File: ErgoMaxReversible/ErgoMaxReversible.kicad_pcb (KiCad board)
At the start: 2 copper layers, 182.8 x 169.2 mm, 106 parts, among them J1 PJ-320A, K1 KEYSW, K10 KEYSW, K11 KEYSW, K12 KEYSW, K13 KEYSW, K14 KEYSW, K15 KEYSW, K16 KEYSW, K17 KEYSW, K18 KEYSW, K19 KEYSW, K2 KEYSW, K20 KEYSW, K21 KEYSW, K22 KEYSW, K23 KEYSW, K24 KEYSW, K25 KEYSW, K26 KEYSW, K27 KEYSW, K28 KEYSW, K29 KEYSW, K3 KEYSW, K30 KEYSW, K31 KEYSW, K32 KEYSW, K33 KEYSW, K34 KEYSW, K35 KEYSW, K36 KEYSW, K37 KEYSW, K38 KEYSW, K39 KEYSW, K4 KEYSW, K40 KEYSW, K41 KEYSW, K42 KEYSW, K43 KEYSW, K44 KEYSW, K5 KEYSW, K6 KEYSW, K7 KEYSW, K8 KEYSW, K9 KEYSW, U1 ProMicro

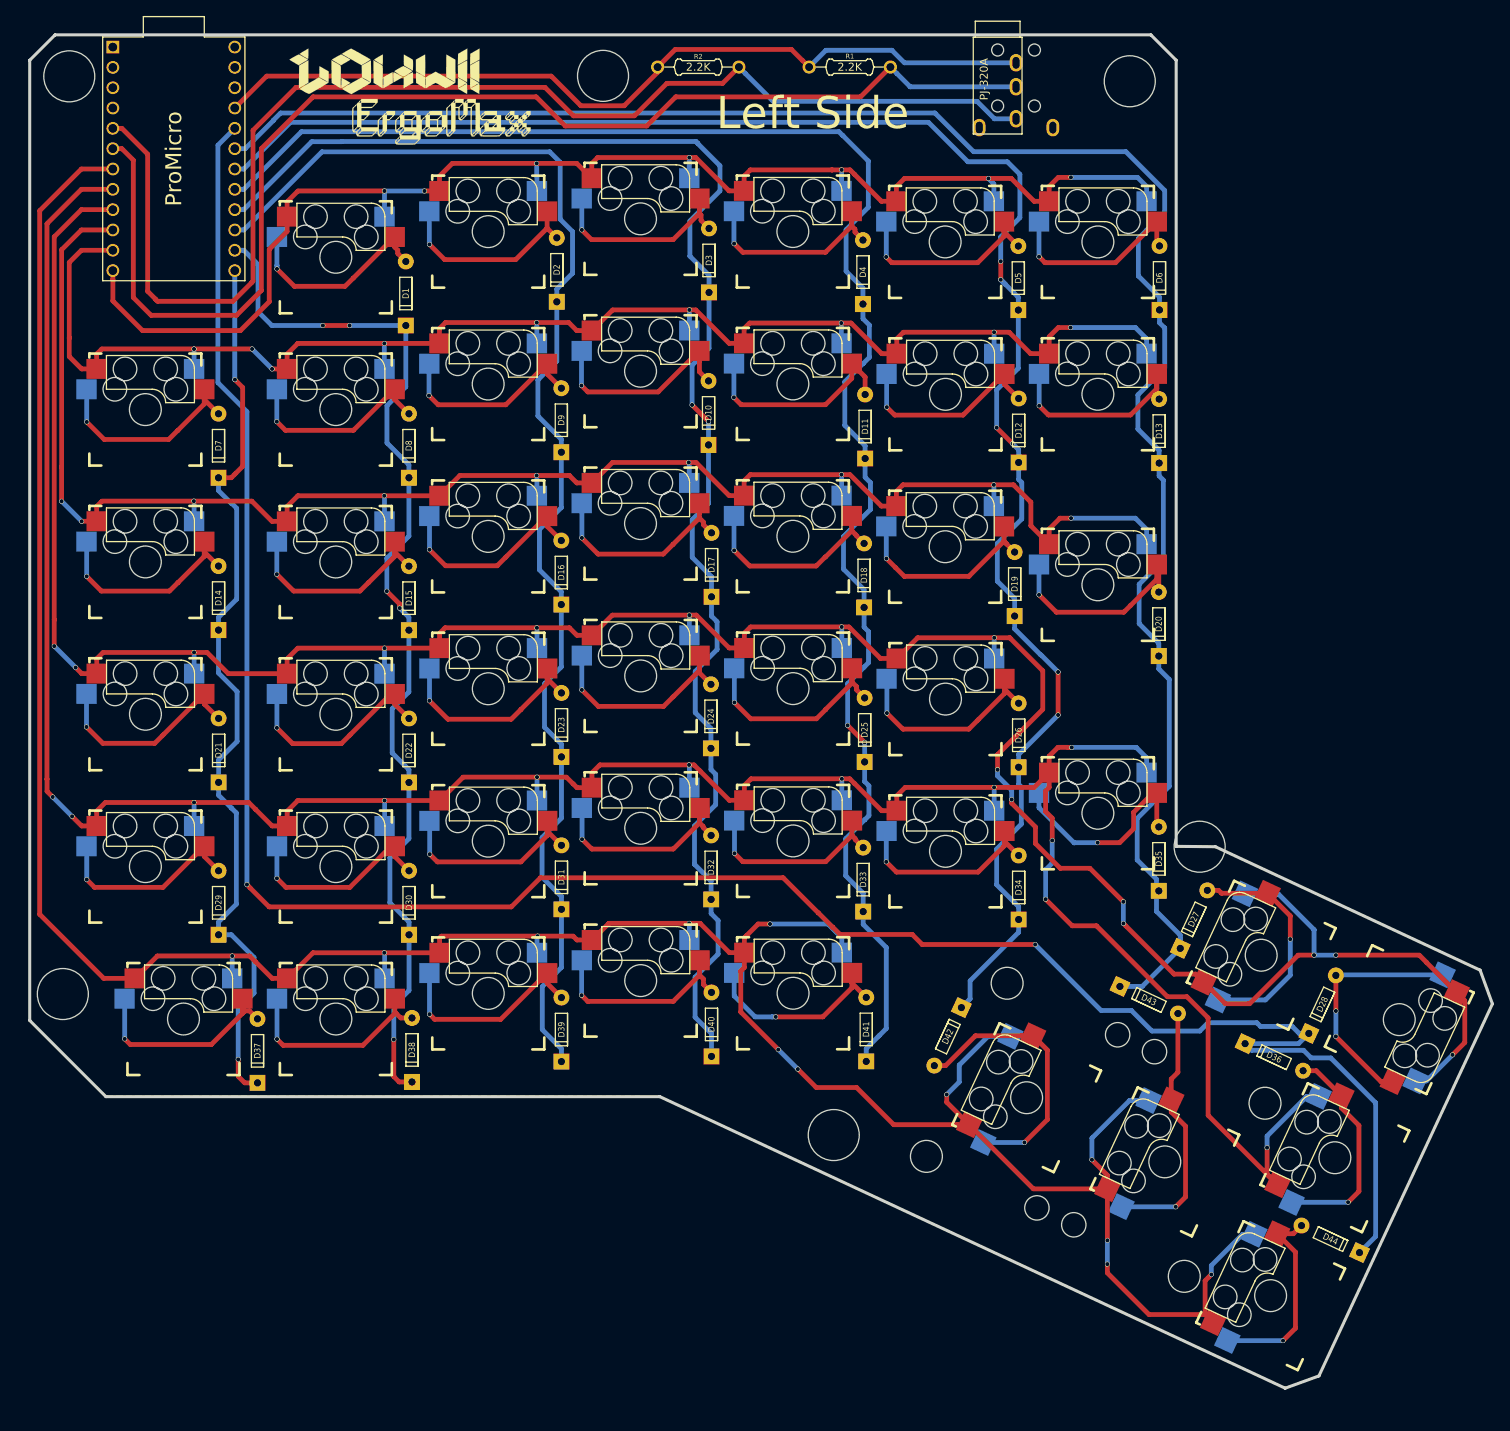
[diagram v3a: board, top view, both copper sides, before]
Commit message: Make reversible PCB use 5 pin hot swap footprint
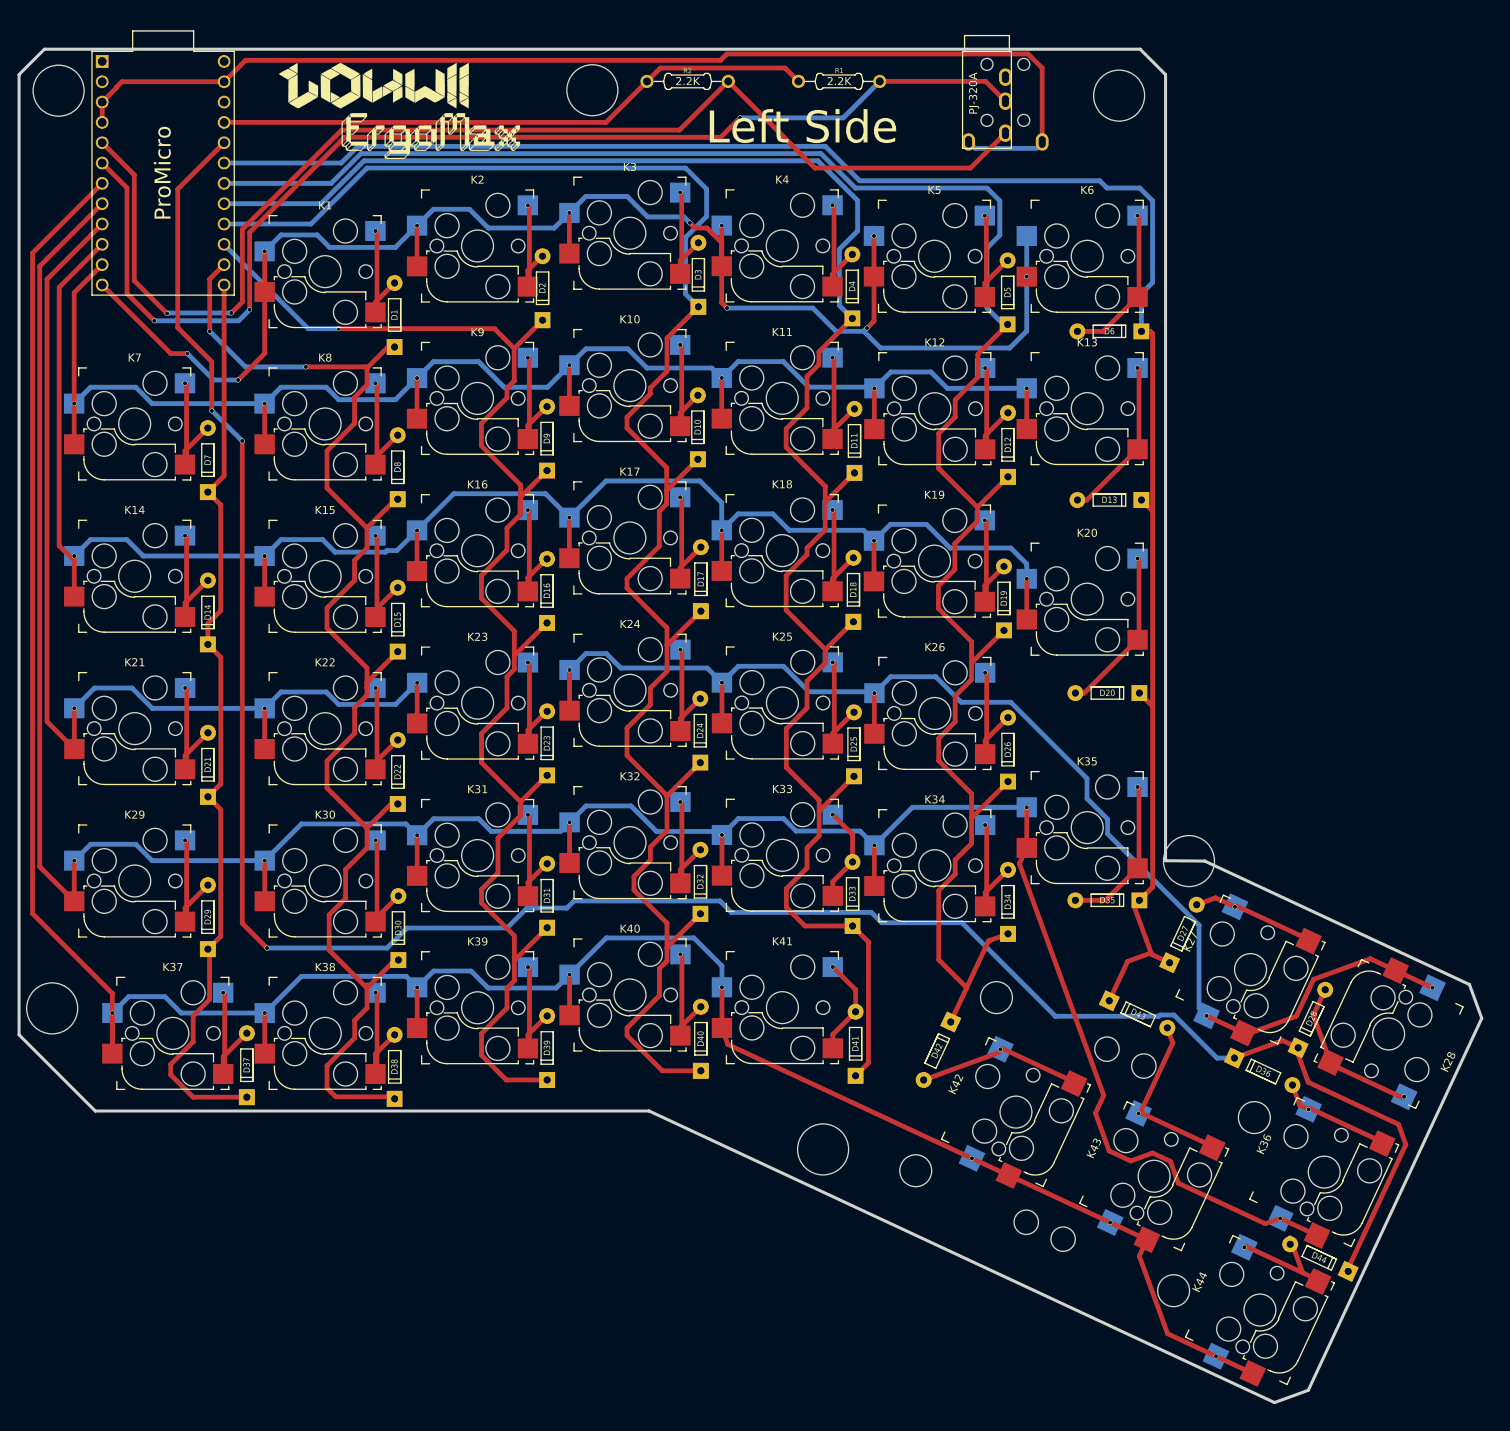
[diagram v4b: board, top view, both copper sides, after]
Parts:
- K1, K10, K11, K12, K13, K14, K15, K16, K17, K18, K19, K2, K20, K21, K22, K23, K24, K25, K26, K27, K28, K29, K3, K30, K31, K32, K33, K34, K35, K36, K37, K38, K39, K4, K40, K41, K42, K43, K44, K5, K6, K7, K8, K9: footprint ErgoMax:Kailh_MX_Socket_reversible -> ErgoMax:Kailh_socket_MX_reversible
- moved D20 10.8 mm to (245.0, 118.1), turned to 0 degrees
- moved D13 10.6 mm to (245.3, 94.0), turned to 0 degrees
- moved D6 9.15 mm to (245.3, 72.9), turned to 0 degrees
- moved D35 8.26 mm to (245.0, 144.0), turned to 0 degrees
- moved D30 3.43 mm to (156.4, 147.5)
- moved D8 3.03 mm to (156.3, 89.9)
- moved D1 3.03 mm to (155.9, 70.9)
- moved D22 3.03 mm to (156.3, 128.0)
- moved D15 3.03 mm to (156.3, 109.0)
- moved D38 3.02 mm to (156.0, 164.8)
- moved D9 2.91 mm to (175.0, 86.3)
- moved D31 2.91 mm to (175.0, 143.5)
- moved D16 2.91 mm to (175.0, 105.4)
- moved D23 2.91 mm to (175.0, 124.4)
- moved D39 2.91 mm to (175.0, 162.5)
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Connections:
- U1 pad 1: Net-(U1-Pad1) -> unconnected-(U1-Pad1)
- U1 pad 2: Net-(U1-Pad2) -> unconnected-(U1-Pad2)
- U1 pad 22: Net-(U1-Pad22) -> unconnected-(U1-Pad22)
- U1 pad 24: Net-(U1-Pad24) -> unconnected-(U1-Pad24)
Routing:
- net GND: track 0.00 -> 141.4 mm
- net /Row3: track 340.0 -> 292.5 mm, vias 15 -> 8
- net /Row5: track 362.0 -> 315.1 mm, vias 12 -> 8
- net /Col1: track 134.1 -> 174.7 mm, vias 5 -> 2
- net /Col3: track 189.8 -> 225.8 mm, vias 2 -> 0
- net VCC: track 106.6 -> 75.3 mm
- net /Col4: track 210.4 -> 234.1 mm, vias 2 -> 0
- net /Col5: track 225.4 -> 248.5 mm, vias 6 -> 0
- net Net-(D27-Pad2): track 29.4 -> 15.5 mm
- net Net-(D25-Pad2): track 29.2 -> 15.3 mm
- net Net-(D36-Pad2): track 27.9 -> 14.2 mm
- net /Row4: track 344.0 -> 330.3 mm, vias 12 -> 8
- net Net-(D33-Pad2): track 25.8 -> 12.2 mm
- net Net-(D42-Pad2): track 34.3 -> 20.8 mm
- net Net-(D41-Pad2): track 25.8 -> 12.5 mm
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- removed copper zone on B.Cu, net GND
- removed copper zone on F.Cu, net GND

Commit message: Fix last net connection
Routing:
- net /Row3: track 292.5 -> 314.7 mm
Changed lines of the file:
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@@
   (segment (start 179.868626 113.19298) (end 182.417764 113.19298) (width 0.6) (layer "B.Cu") (net 56))
   (segment (start 141.760214 117.987778) (end 147.401072 117.987778) (width 0.6) (layer "B.Cu") (net 56))
+  (segment (start 174.831628 112.255984) (end 177.818625 115.242981) (width 0.6) (layer "B.Cu") (net 56))
   (segment (start 215.91861 118.136582) (end 217.968611 116.086581) (width 0.6) (layer "B.Cu") (net 56))
   (segment (start 184.224784 115) (end 195.042873 115) (width 0.6) (layer "B.Cu") (net 56))
@@
   (segment (start 223.586581 116.086581) (end 226.775681 119.275681) (width 0.6) (layer "B.Cu") (net 56))
   (segment (start 242.5 128.8036) (end 242.5 131.319502) (width 0.6) (layer "B.Cu") (net 56))
+  (segment (start 163.35862 112.255984) (end 174.831628 112.255984) (width 0.6) (layer "B.Cu") (net 56))
   (segment (start 198.918617 114.775742) (end 204.559475 114.775742) (width 0.6) (layer "B.Cu") (net 56))
   (segment (start 195.042873 115) (end 196.868616 116.825743) (width 0.6) (layer "B.Cu") (net 56))
@@
   (segment (start 177.818625 115.242981) (end 179.868626 113.19298) (width 0.6) (layer "B.Cu") (net 56))
   (segment (start 196.868616 116.825743) (end 198.918617 114.775742) (width 0.6) (layer "B.Cu") (net 56))
+  (segment (start 158.768619 116.845985) (end 163.35862 112.255984) (width 0.6) (layer "B.Cu") (net 56))
   (segment (start 250.695978 175.624179) (end 247.966493 176.617636) (width 0.6) (layer "F.Cu") (net 57))
   (segment (start 111.595201 139.842325) (end 115.908614 144.155738) (width 0.6) (layer "F.Cu") (net 57))

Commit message: Fix net
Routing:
- net VCC: track 75.3 -> 102.4 mm
- net SDA: track 153.1 -> 150.2 mm
- net /Row1: track 187.4 -> 188.7 mm
- net /Row2: track 218.1 -> 218.6 mm
- added copper zone on B.Cu, net GND
- added copper zone on F.Cu, net GND
